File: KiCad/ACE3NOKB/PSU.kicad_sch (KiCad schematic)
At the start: 30 parts

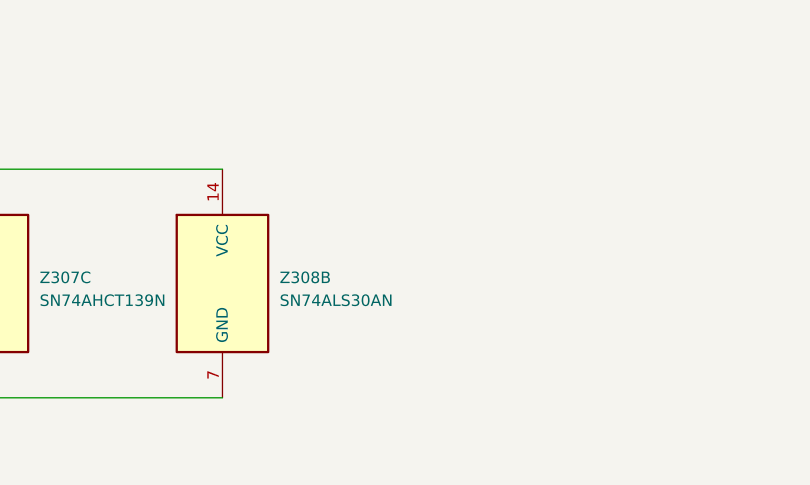
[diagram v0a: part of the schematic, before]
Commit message: First complete system. Unlikely to work but will serve as the basis of a system to test VGA.
Signed-off-by: John Bradley <flypie@rocketmail.com>
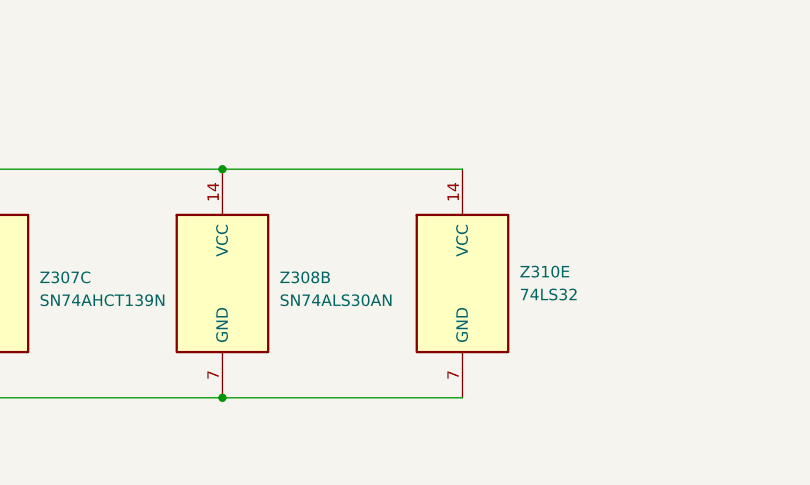
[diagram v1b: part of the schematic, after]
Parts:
- added Z310: 74LS32, Package_DIP:DIP-14_W7.62mm, symbol 74xx:74LS32
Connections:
- net GND: now also Z310.7 (GND)
- net VCC: now also Z310.14 (VCC)
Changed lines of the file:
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@@
     (comment 4 "This work is licensed under a Creative Commons ")
   )
+  (junction (at 153.67 158.75) (diameter 0) (color 0 0 0 0)
+  )
   (junction (at 101.6 82.55) (diameter 0) (color 0 0 0 0)
   )
@@
   )
   (junction (at 50.8 107.95) (diameter 0) (color 0 0 0 0)
+  )
+  (junction (at 153.67 133.35) (diameter 0) (color 0 0 0 0)
   )
   (junction (at 88.9 50.8) (diameter 0) (color 0 0 0 0)
@@
     (stroke (width 0) (type default) (color 0 0 0 0))
   )
+  (wire (pts (xy 153.67 158.75) (xy 180.34 158.75))
+    (stroke (width 0) (type default) (color 0 0 0 0))
+  )
   (wire (pts (xy 50.8 60.96) (xy 50.8 63.5))
     (stroke (width 0) (type default) (color 0 0 0 0))
@@
   )
   (wire (pts (xy 139.7 63.5) (xy 152.4 63.5))
+    (stroke (width 0) (type default) (color 0 0 0 0))
+  )
+  (wire (pts (xy 153.67 133.35) (xy 180.34 133.35))
     (stroke (width 0) (type default) (color 0 0 0 0))
   )
@@
     (pin "1")
   )
+  (symbol (lib_id "74xx:74LS32") (at 180.34 146.05 0) (unit 5)
+    (in_bom yes) (on_board yes) (fields_autoplaced)
+    (property "Reference" "Z310" (id 0) (at 186.69 144.7799 0)
+      (effects (font (size 1.27 1.27)) (justify left))
+    )
+    (property "Value" "74LS32" (id 1) (at 186.69 147.3199 0)
+      (effects (font (size 1.27 1.27)) (justify left))
+    )
+    (property "Footprint" "Package_DIP:DIP-14_W7.62mm" (id 2) (at 180.34 146.05 0)
+      (effects (font (size 1.27 1.27)) hide)
+    )
+    (property "Datasheet" "http://www.ti.com/lit/gpn/sn74LS32" (id 3) (at 180.34 146.05 0)
+      (effects (font (size 1.27 1.27)) hide)
+    )
+    (pin "1")
+    (pin "2")
+    (pin "3")
+    (pin "4")
+    (pin "5")
+    (pin "6")
+    (pin "10")
+    (pin "8")
+    (pin "9")
+    (pin "11")
+    (pin "12")
+    (pin "13")
+    (pin "14")
+    (pin "7")
+  )
 )

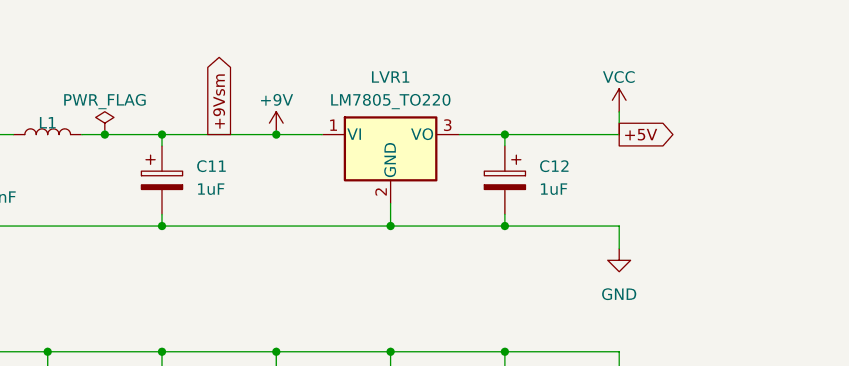
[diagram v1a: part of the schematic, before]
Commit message: Update to latest symbols. Change name of Data Bus from DA to D.
Signed-off-by: John Bradley <flypie@rocketmail.com>
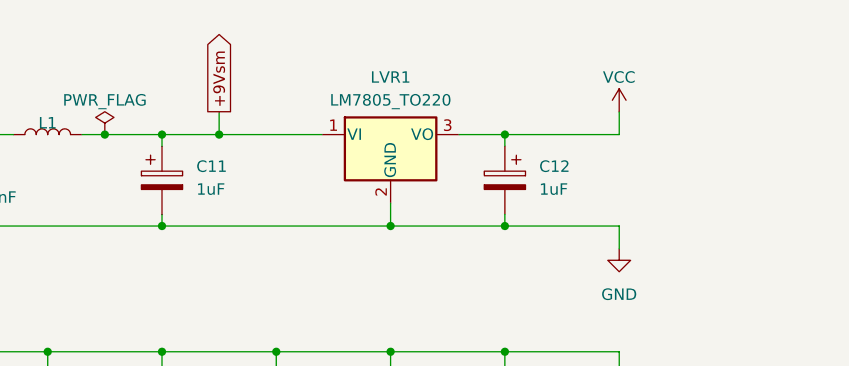
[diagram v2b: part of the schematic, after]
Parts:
- 9V-DC1: footprint ExtraFootprints:163179PHEX -> 163179PHEX
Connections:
- net +9V renamed +9Vsm
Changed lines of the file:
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@@
   (junction (at 76.2 107.95) (diameter 0) (color 0 0 0 0)
   )
-  (junction (at 114.3 26.67) (diameter 0) (color 0 0 0 0)
+  (junction (at 107.95 26.67) (diameter 0) (color 0 0 0 0)
   )
   (junction (at 127 63.5) (diameter 0) (color 0 0 0 0)
   )
   (no_connect (at 38.1 33.02))
-  (wire (pts (xy 101.6 26.67) (xy 114.3 26.67))
+  (wire (pts (xy 101.6 26.67) (xy 107.95 26.67))
     (stroke (width 0) (type default) (color 0 0 0 0))
   )
@@
     (stroke (width 0) (type default) (color 0 0 0 0))
   )
+  (wire (pts (xy 107.95 24.13) (xy 107.95 26.67))
+    (stroke (width 0) (type default) (color 0 0 0 0))
+  )
   (wire (pts (xy 101.6 36.83) (xy 127 36.83))
     (stroke (width 0) (type default) (color 0 0 0 0))
@@
     (stroke (width 0) (type default) (color 0 0 0 0))
   )
-  (wire (pts (xy 114.3 26.67) (xy 119.38 26.67))
+  (wire (pts (xy 107.95 26.67) (xy 119.38 26.67))
     (stroke (width 0) (type default) (color 0 0 0 0))
   )
@@
     (effects (font (size 1.27 1.27)) (justify left bottom))
   )
-  (global_label "+5V" (shape output) (at 152.4 26.67 0) (fields_autoplaced)
+  (global_label "+9Vsm" (shape output) (at 107.95 24.13 90) (fields_autoplaced)
     (effects (font (size 1.27 1.27)) (justify left))
-    (property "Intersheet References" "${INTERSHEET_REFS}" (id 0) (at 158.5947 26.5906 0)
-      (effects (font (size 1.27 1.27)) (justify left))
-    )
-  )
-  (global_label "+9Vsm" (shape output) (at 107.95 26.67 90) (fields_autoplaced)
-    (effects (font (size 1.27 1.27)) (justify left))
-    (property "Intersheet References" "${INTERSHEET_REFS}" (id 0) (at 107.8706 17.7539 90)
+    (property "Intersheet References" "${INTERSHEET_REFS}" (id 0) (at 107.8706 15.2139 90)
       (effects (font (size 1.27 1.27)) (justify left))
     )
@@
     (property "Reference" "9V-DC1" (id 0) (at 48.26 24.13 0))
     (property "Value" "163-179PH-EX " (id 1) (at 48.26 26.67 0))
-    (property "Footprint" "ExtraFootprints:163179PHEX" (id 2) (at 54.61 35.56 0)
+    (property "Footprint" "163179PHEX" (id 2) (at 54.61 35.56 0)
       (effects (font (size 1.27 1.27)) (justify left) hide)
     )
@@
       (effects (font (size 1.27 1.27)) hide)
     )
-    (pin "1")
-  )
-  (symbol (lib_id "power:+9V") (at 114.3 26.67 0) (unit 1)
-    (in_bom yes) (on_board yes) (fields_autoplaced)
-    (property "Reference" "#~PWR0162" (id 0) (at 114.3 30.48 0)
-      (effects (font (size 1.27 1.27)) hide)
-    )
-    (property "Value" "+9V" (id 1) (at 114.3 22.86 0))
-    (property "Footprint" "" (id 2) (at 114.3 26.67 0)
-      (effects (font (size 1.27 1.27)) hide)
-    )
-    (property "Datasheet" "" (id 3) (at 114.3 26.67 0)
-      (effects (font (size 1.27 1.27)) hide)
-    )

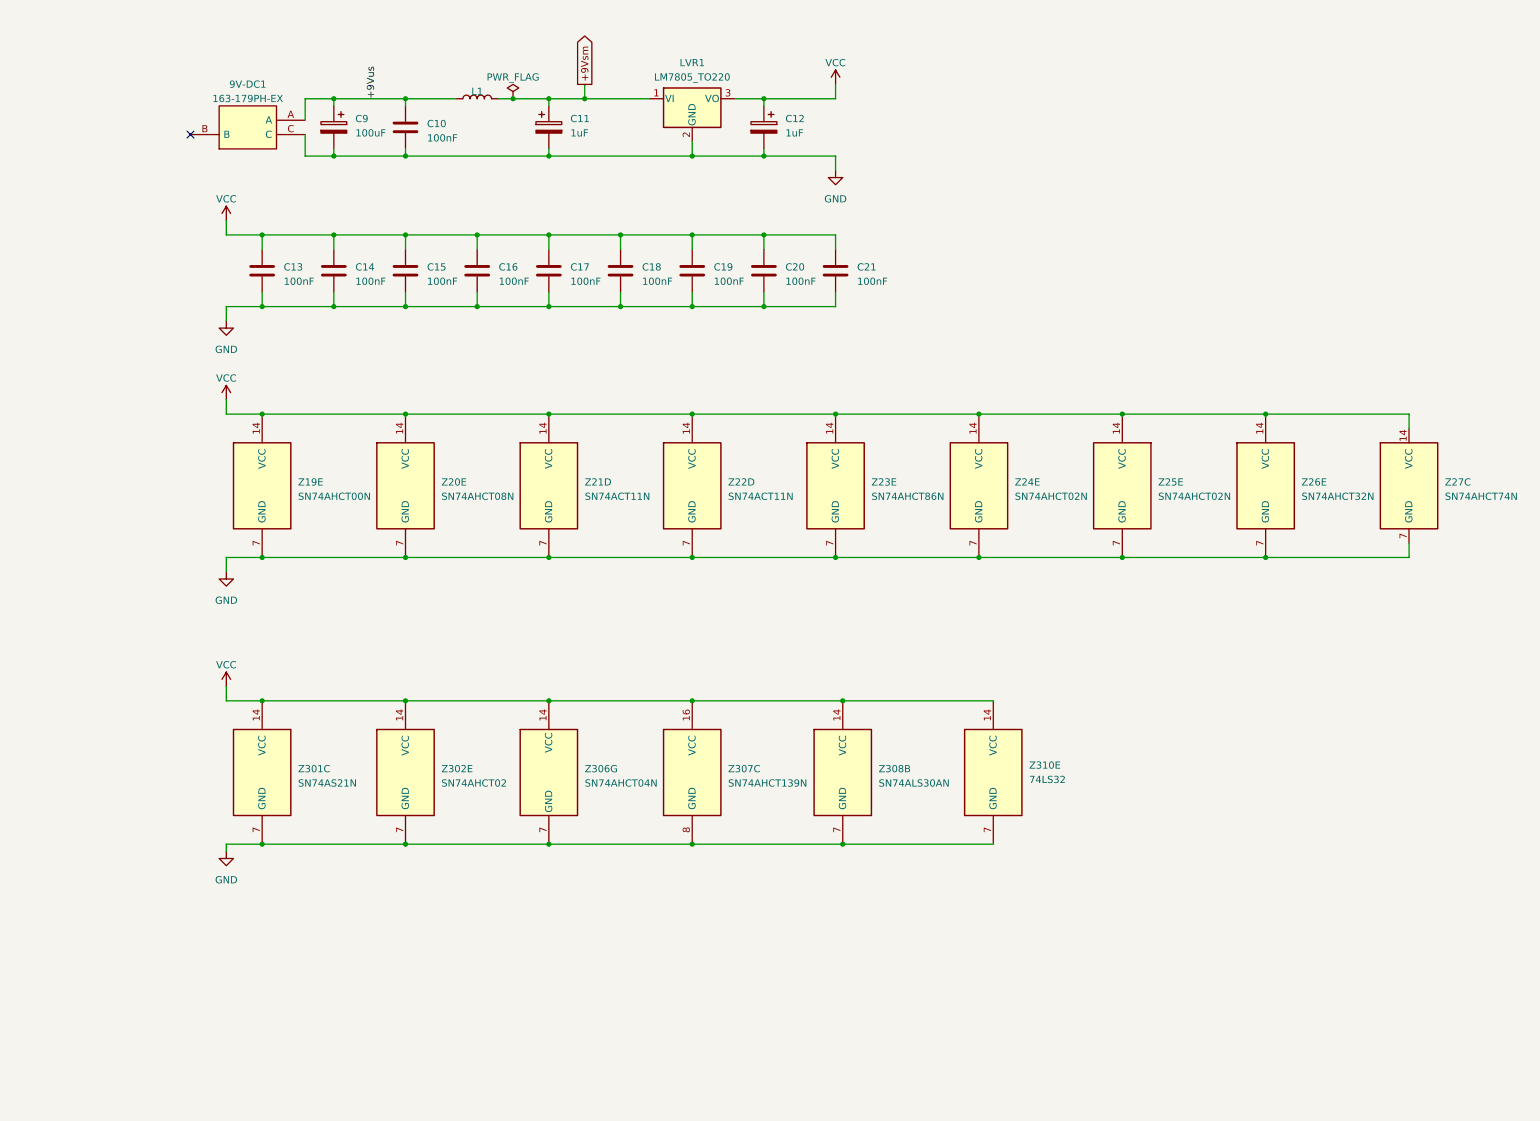
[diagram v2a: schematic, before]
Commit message: Consolidation with increased configuration of speed and Int Routing to allow Orginal ACE ROM.
Signed-off-by: John Bradley <flypie@rocketmail.com>
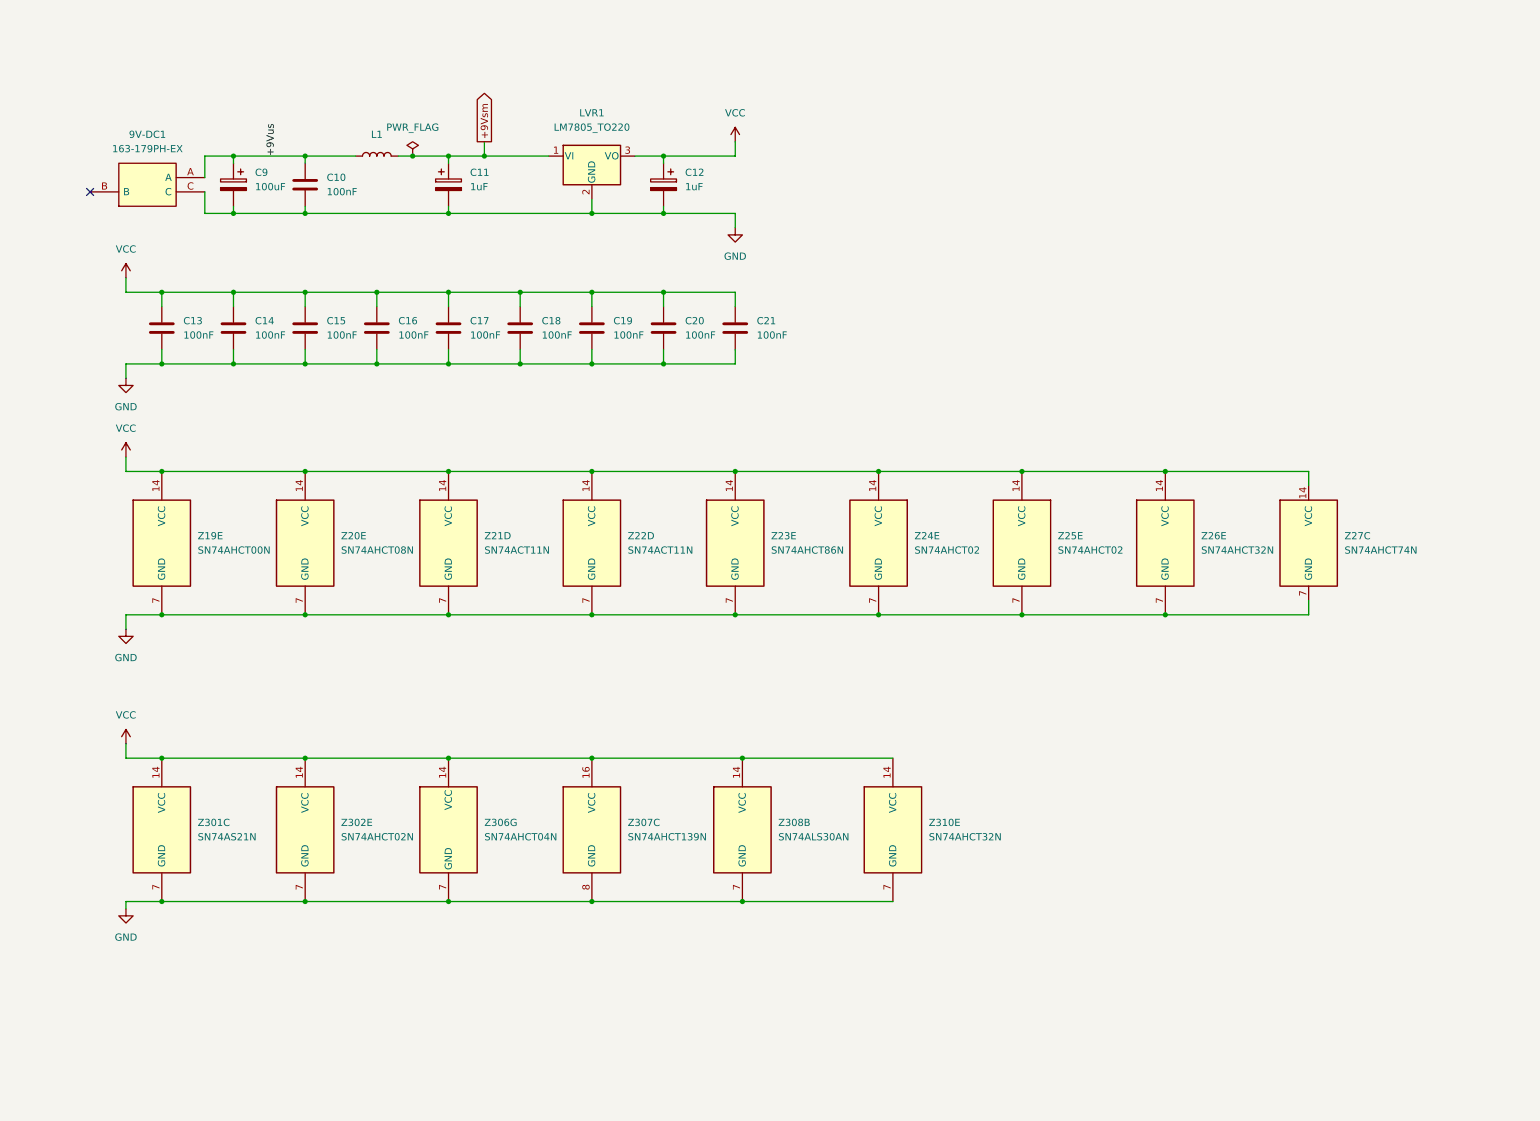
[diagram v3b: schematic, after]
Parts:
- 9V-DC1: Manufacturer_Name Kobiconn -> (none); Manufacturer_Part_Number 163-179PH-EX -> (none); Mouser Price/Stock https://www.mouser.co.uk/ProductDetail/Kobiconn/163-179PH-E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 -> (none)
- C10, C13, C14, C15, C16, C17, C18, C19, C20, C21: footprint Capacitor_THT:C_Disc_D5.0mm_W2.5mm_P5.00mm -> Capacitor_THT:C_Disc_D3.0mm_W1.6mm_P2.50mm; Manufacturer_Name Vishay -> (none); Manufacturer_Part_Number K104K15X7RF53H5 -> (none)
- C11, C12, C9: Manufacturer_Name Lelon -> (none); Manufacturer_Part_Number REA101M1CBK-0611P -> (none)
- L1: value EMI_Filter_LL_1423 -> 4.7uH to 100uH.; footprint ExtraFootprints:KEMET_SBT_0260T -> Inductor_THT:L_Axial_L6.6mm_D2.7mm_P2.54mm_Vertical_Vishay_IM-2; Manufacturer_Name KEMET -> (none); Manufacturer_Part_Number SBT-0260 -> (none)
- LVR1: footprint Package_TO_SOT_THT:TO-220-3_Vertical -> ExtraFootprints:TO-220-3_Horizontal_TabDown_HS; Manufacturer_Name texas instruments -> (none); Manufacturer_Part_Number LM7805CT/NOPB -> (none)
- Z19: Manufacturer_Name Texas Instruments -> (none); Manufacturer_Part_Number SN74AHCT00N -> (none)
- Z20: Manufacturer_Name Texas Instruments -> (none); Manufacturer_Part_Number SN74AHCT08N -> (none)
- Z21, Z22: Manufacturer_Name Texas Instruments -> (none); Manufacturer_Part_Number SN74ACT11N -> (none)
- Z23: Manufacturer_Name Texas Instruments -> (none); Manufacturer_Part_Number SN74AHCT86N -> (none)
- Z24, Z25: value SN74AHCT02N -> SN74AHCT02; Manufacturer_Name Texas Instruments -> (none); Manufacturer_Part_Number SN74AHCT02N -> (none)
- Z26: Manufacturer_Name Texas Instruments -> (none); Manufacturer_Part_Number SN74AHCT32N -> (none)
- Z27: Manufacturer_Name Texas Instruments -> (none); Manufacturer_Part_Number SN74AHCT74N -> (none)
- Z301: Manufacturer_Name Texas Instruments -> (none); Manufacturer_Part_Number SN74AS21N -> (none)
- Z302: value SN74AHCT02 -> SN74AHCT02N; Manufacturer_Name Texas Instruments -> (none); Manufacturer_Part_Number SN74AHCT32N -> (none)
- Z306: Manufacturer_Name Texas Instruments -> (none); Manufacturer_Part_Number SN74AHCT04N -> (none)
- Z307: Manufacturer_Name Texas Instruments -> (none); Manufacturer_Part_Number SN74AHCT139N -> (none)
- Z308: Manufacturer_Name Texas Instruments -> (none); Manufacturer_Part_Number SN74ALS30AN -> (none)
- Z310: value 74LS32 -> SN74AHCT32N
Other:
- moved on the sheet: 9V-DC1, C10, C11, C12, C13, C14, C15, C16, C17, C18, C19, C20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

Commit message: Update to last expermintal version. Uses clock sythsiser and can be switched between full ACE compatible and inhanced IO. Should be able to switch between multiple ROM images tosred on the same chip.
Signed-off-by: John Bradley <flypie@rocketmail.com>
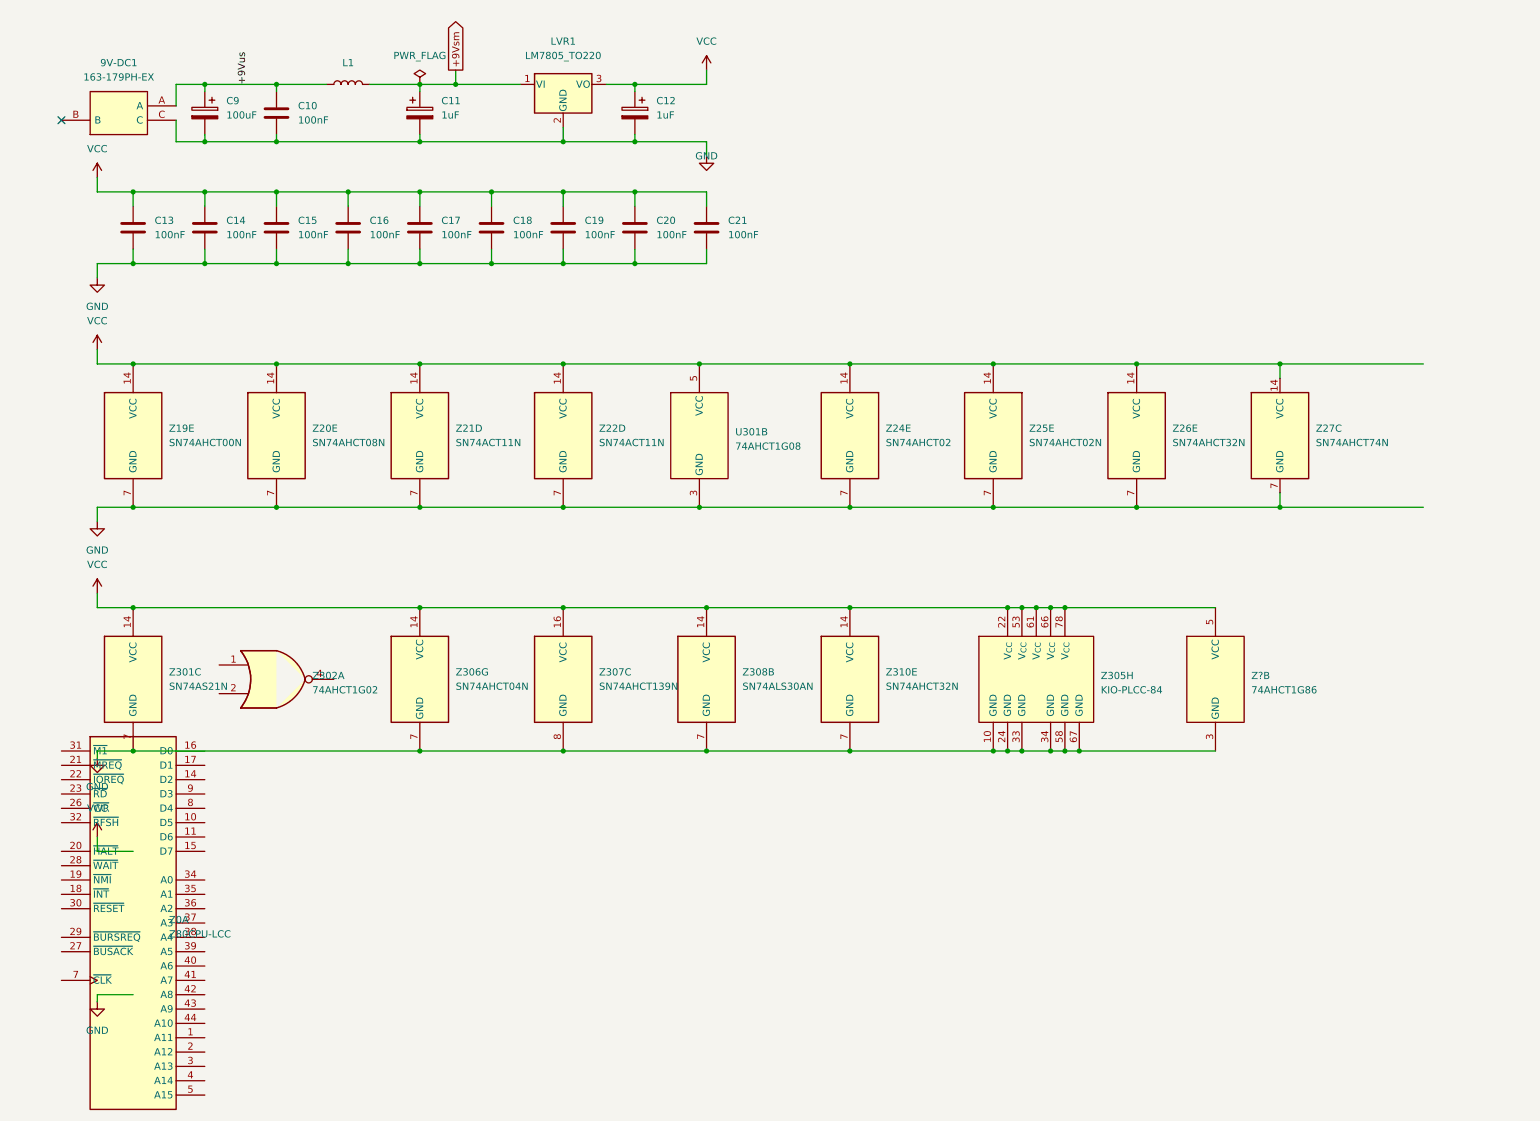
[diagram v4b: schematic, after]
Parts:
- removed Z23: SN74AHCT86N, Package_DIP:DIP-14_W7.62mm, symbol 74xx:74LS86
- removed Z302: SN74AHCT02N, Package_DIP:DIP-14_W7.62mm, symbol 74xx:74LS02
- added U301: 74AHCT1G08, Package_TO_SOT_SMD:SOT-23-5, symbol 74xGxx:74AHCT1G08
- added Z0: Z80CPU-LCC, ExtraFootprints:PLCC-44_THT-Socket, symbol CPU_Zilog_Z80:Z80CPU-PLCC
- added Z302: 74AHCT1G02, Package_TO_SOT_SMD:SOT-23-5_HandSoldering, symbol 74xGxx:74AHCT1G02
- added Z305: KIO-PLCC-84, ExtraFootprints:PLCC-84_THT-Socket, symbol CPU_Zilog_Z80_Peripherals_Units:Z8490-KIO-PLCC-84-UNITS
- added Z?: 74AHCT1G86, Package_TO_SOT_SMD:SOT-23-5, symbol 74xGxx:74AHCT1G86
- 9V-DC1: footprint 163179PHEX -> ExtraFootprints:163179PHEX; Manufacturer_Name (none) -> Kobiconn; Manufacturer_Part_Number (none) -> 163-179PH-EX; Mouser Price/Stock (none) -> https://www.mouser.co.uk/ProductDetail/Kobiconn/163-179PH-E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
- LVR1: footprint ExtraFootprints:TO-220-3_Horizontal_TabDown_HS -> Package_TO_SOT_THT:TO-220-3_Horizontal_TabDown
- Z25: value SN74AHCT02 -> SN74AHCT02N
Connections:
- net GND: now also U301.3 (GND), Z305.10 (GND), Z305.24 (GND), Z305.33 (GND), Z305.34 (GND), Z305.58 (GND), Z305.67 (GND), Z?.3 (GND)
- net VCC: now also U301.5 (VCC), Z305.22 (V_{CC}), Z305.53 (V_{CC}), Z305.61 (V_{CC}), Z305.66 (V_{CC}), Z305.78 (V_{CC}), Z?.5 (VCC)
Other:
- moved on the sheet: 9V-DC1, C10, C11, C12, C13, C14, C15, C16, C17, C18, C19, C20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
